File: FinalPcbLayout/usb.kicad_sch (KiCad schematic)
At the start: 5 parts, among them J5 USB_C_Receptacle, Q2 S8050, Q3 S8050

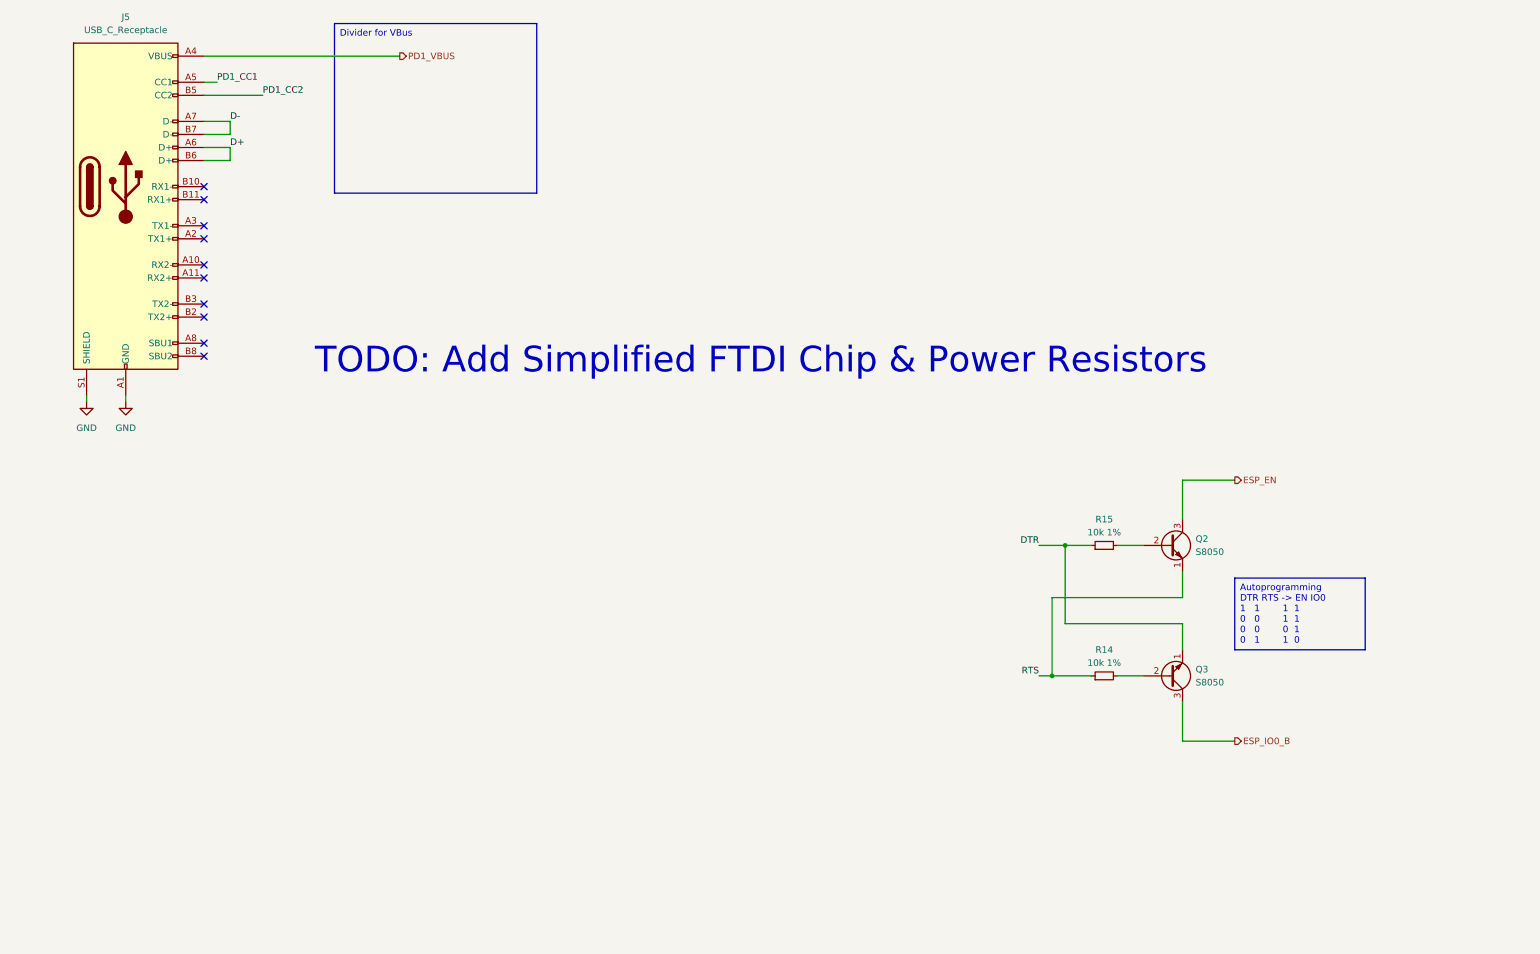
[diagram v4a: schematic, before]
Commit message: Found A Good USB-To-Uart
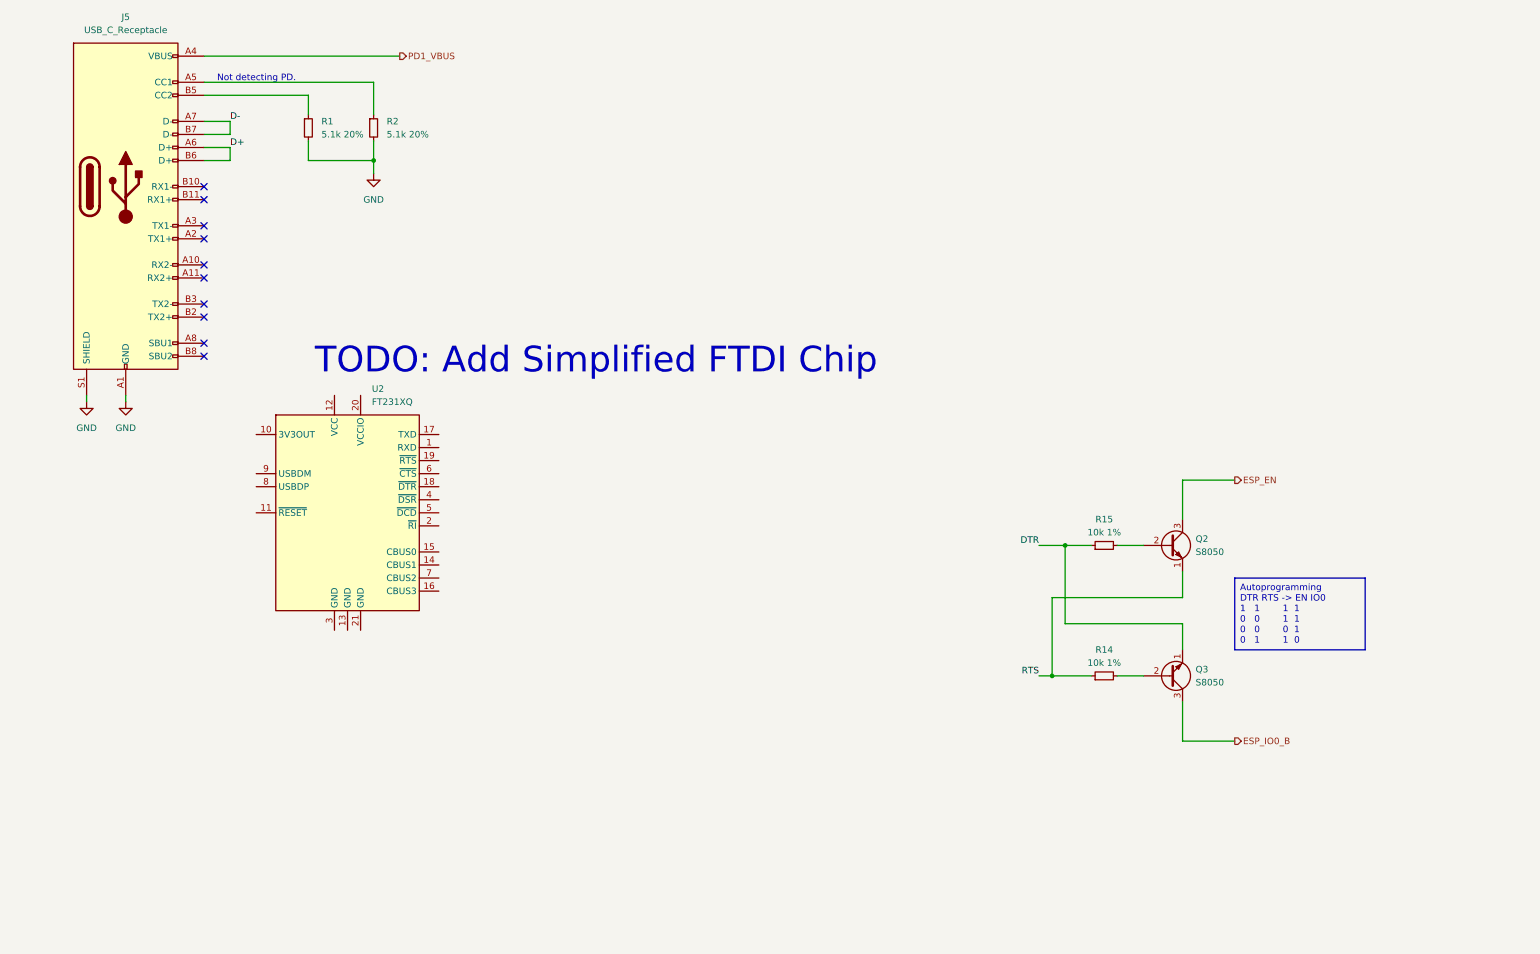
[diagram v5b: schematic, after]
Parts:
- added R1, R2: 5.1k 20%, symbol Device:R_Small
- added U2: FT231XQ, Package_DFN_QFN:QFN-20-1EP_4x4mm_P0.5mm_EP2.5x2.5mm, symbol Interface_USB:FT231XQ
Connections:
- net GND: now also R1.2, R2.2
- net PD1_CC1: no longer names the net of J5.A5 (CC1)
- net PD1_CC1: now also R2.1
- net PD1_CC2: no longer names the net of J5.B5 (CC2)
- net PD1_CC2: now also R1.1
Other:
- note added: "Not detecting PD."
- note added: "TODO: Add Simplified FTDI Chip"
- note removed: "TODO: Add Simplified FTDI Chip & Power Resistors"
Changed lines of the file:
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@@
     (comment 1 "Author: Jake Armstrong")
+  )
+  (junction (at 83.82 41.91) (diameter 0) (color 0 0 0 0)
   )
   (junction (at 215.9 142.24) (diameter 0) (color 0 0 0 0)
@@
     (stroke (width 0) (type default))
   )
+  (wire (pts (xy 71.12 38.1) (xy 71.12 41.91))
+    (stroke (width 0) (type default))
+  )
   (wire (pts (xy 251.46 154.94) (xy 241.3 154.94))
     (stroke (width 0) (type default))
   )
+  (wire (pts (xy 83.82 38.1) (xy 83.82 41.91))
+    (stroke (width 0) (type default))
+  )
+  (wire (pts (xy 83.82 41.91) (xy 83.82 44.45))
+    (stroke (width 0) (type default))
+  )
   (wire (pts (xy 55.88 34.29) (xy 50.8 34.29))
     (stroke (width 0) (type default))
@@
     (stroke (width 0) (type default))
   )
+  (wire (pts (xy 71.12 33.02) (xy 71.12 29.21))
+    (stroke (width 0) (type default))
+  )
+  (wire (pts (xy 71.12 41.91) (xy 83.82 41.91))
+    (stroke (width 0) (type default))
+  )
   (wire (pts (xy 50.8 36.83) (xy 55.88 36.83))
     (stroke (width 0) (type default))
@@
     (stroke (width 0) (type default))
   )
-  (wire (pts (xy 50.8 29.21) (xy 62.23 29.21))
+  (wire (pts (xy 50.8 29.21) (xy 71.12 29.21))
     (stroke (width 0) (type default))
   )
@@
     (stroke (width 0) (type default))
   )
+  (wire (pts (xy 83.82 26.67) (xy 83.82 33.02))
+    (stroke (width 0) (type default))
+  )
   (wire (pts (xy 55.88 39.37) (xy 50.8 39.37))
     (stroke (width 0) (type default))
@@
     (stroke (width 0) (type default))
   )
-  (wire (pts (xy 50.8 26.67) (xy 53.34 26.67))
+  (wire (pts (xy 50.8 26.67) (xy 83.82 26.67))
     (stroke (width 0) (type default))
   )
@@
     (effects (font (size 1.27 1.27)) (justify left top))
   )
-  (text_box "Divider for VBus\n"
-    (at 76.2 15.24 0) (size 39.37 33.02)
-    (stroke (width 0) (type default))
-    (fill (type none))
-    (effects (font (size 1.27 1.27)) (justify left top))
-  )
-  (text "TODO: Add Simplified FTDI Chip & Power Resistors" (at 72.39 83.82 0)
+  (text "TODO: Add Simplified FTDI Chip\n" (at 72.39 83.82 0)
     (effects (font (size 5 5)) (justify left bottom))
+  )
+  (text "Not detecting PD.\n" (at 53.34 26.67 0)
+    (effects (font (size 1.27 1.27)) (justify left bottom))
   )
   (label "D+" (at 55.88 39.37 0) (fields_autoplaced)
@@
     (effects (font (size 1.27 1.27)) (justify right bottom))
   )
-  (label "PD1_CC2" (at 62.23 29.21 0) (fields_autoplaced)
-    (effects (font (size 1.27 1.27)) (justify left bottom))
-  )
   (label "D-" (at 55.88 34.29 0) (fields_autoplaced)
     (effects (font (size 1.27 1.27)) (justify left bottom))
@@
     (effects (font (size 1.27 1.27)) (justify right bottom))
   )
-  (label "PD1_CC1" (at 53.34 26.67 0) (fields_autoplaced)
-    (effects (font (size 1.27 1.27)) (justify left bottom))
-  )
   (hierarchical_label "ESP_IO0_B" (shape output) (at 251.46 154.94 0) (fields_autoplaced)
     (effects (font (size 1.27 1.27)) (justify left))
@@
         (path "/9fcc273e-b318-4ade-b4c7-fe4ddbf9d677/80fb5872-9ff7-41e5-9921-84d432e9852e"
           (reference "Q3") (unit 1)
+        )
+      )
+    )
+  )
+  (symbol (lib_id "power:GND") (at 83.82 44.45 0) (unit 1)
+    (in_bom yes) (on_board yes) (dnp no) (fields_autoplaced)
+    (property "Reference" "#PWR06" (at 83.82 50.8 0)
+      (effects (font (size 1.27 1.27)) hide)
+    )
+    (property "Value" "GND" (at 83.82 49.53 0)
+      (effects (font (size 1.27 1.27)))
+    )
+    (property "Footprint" "" (at 83.82 44.45 0)
+      (effects (font (size 1.27 1.27)) hide)
+    )
+    (property "Datasheet" "" (at 83.82 44.45 0)
+      (effects (font (size 1.27 1.27)) hide)
+    )
+    (pin "1")
+    (instances
+      (project "FinalPcbLayout"
+        (path "/9fcc273e-b318-4ade-b4c7-fe4ddbf9d677/80fb5872-9ff7-41e5-9921-84d432e9852e"
+          (reference "#PWR06") (unit 1)
         )
       )
@@
     )
   )
+  (symbol (lib_id "Device:R_Small") (at 83.82 35.56 0) (unit 1)
+    (in_bom yes) (on_board yes) (dnp no) (fields_autoplaced)
+    (property "Reference" "R2" (at 86.36 34.29 0)
+      (effects (font (size 1.27 1.27)) (justify left))
+    )
+    (property "Value" "5.1k 20%" (at 86.36 36.83 0)
+      (effects (font (size 1.27 1.27)) (justify left))
+    )
+    (property "Footprint" "" (at 83.82 35.56 0)
+      (effects (font (size 1.27 1.27)) hide)
+    )
+    (property "Datasheet" "~" (at 83.82 35.56 0)
+      (effects (font (size 1.27 1.27)) hide)
+    )
+    (pin "2")
+    (pin "1")
+    (instances
+      (project "FinalPcbLayout"
+        (path "/9fcc273e-b318-4ade-b4c7-fe4ddbf9d677/80fb5872-9ff7-41e5-9921-84d432e9852e"
+          (reference "R2") (unit 1)
+        )
+      )
+    )
+  )
   (symbol (lib_id "power:GND") (at 27.94 88.9 0) (unit 1)
     (in_bom yes) (on_board yes) (dnp no) (fields_autoplaced)
@@
         (path "/9fcc273e-b318-4ade-b4c7-fe4ddbf9d677/80fb5872-9ff7-41e5-9921-84d432e9852e"
           (reference "R14") (unit 1)
+        )
+      )
+    )
+  )
+  (symbol (lib_id "Device:R_Small") (at 71.12 35.56 0) (unit 1)
+    (in_bom yes) (on_board yes) (dnp no) (fields_autoplaced)
+    (property "Reference" "R1" (at 73.66 34.29 0)
+      (effects (font (size 1.27 1.27)) (justify left))
+    )
+    (property "Value" "5.1k 20%" (at 73.66 36.83 0)
+      (effects (font (size 1.27 1.27)) (justify left))
+    )
+    (property "Footprint" "" (at 71.12 35.56 0)
+      (effects (font (size 1.27 1.27)) hide)
+    )
+    (property "Datasheet" "~" (at 71.12 35.56 0)
+      (effects (font (size 1.27 1.27)) hide)
+    )
+    (pin "2")
+    (pin "1")
+    (instances
+      (project "FinalPcbLayout"
+        (path "/9fcc273e-b318-4ade-b4c7-fe4ddbf9d677/80fb5872-9ff7-41e5-9921-84d432e9852e"
+          (reference "R1") (unit 1)
         )
       )
@@
         )
       )
+    )
+  )
+  (symbol (lib_id "Interface_USB:FT231XQ") (at 78.74 110.49 0) (unit 1)
+    (in_bom yes) (on_board yes) (dnp no) (fields_autoplaced)
+    (property "Reference" "U2" (at 83.4741 86.36 0)
+      (effects (font (size 1.27 1.27)) (justify left))
+    )
+    (property "Value" "FT231XQ" (at 83.4741 88.9 0)
+      (effects (font (size 1.27 1.27)) (justify left))
+    )
+    (property "Footprint" "Package_DFN_QFN:QFN-20-1EP_4x4mm_P0.5mm_EP2.5x2.5mm" (at 113.03 130.81 0)
+      (effects (font (size 1.27 1.27)) hide)
+    )
+    (property "Datasheet" "https://www.ftdichip.com/Support/Documents/DataSheets/ICs/DS_FT231X.pdf" (at 78.74 110.49 0)
+      (effects (font (size 1.27 1.27)) hide)
+    )
+    (property "digikey_pn" "768-1155-ND" (at 78.74 110.49 0)
+      (effects (font (size 1.27 1.27)) hide)
+    )
+    (pin "12")
+    (pin "4")
+    (pin "19")
+    (pin "9")
+    (pin "15")
+    (pin "13")
+    (pin "1")
+    (pin "20")
+    (pin "17")
+    (pin "11")
+    (pin "2")
+    (pin "21")
+    (pin "3")
+    (pin "10")
+    (pin "5")
+    (pin "6")
+    (pin "7")
+    (pin "14")
+    (pin "16")
+    (pin "18")
+    (pin "8")
+    (instances
+      (project "FinalPcbLayout"
+        (path "/9fcc273e-b318-4ade-b4c7-fe4ddbf9d677/80fb5872-9ff7-41e5-9921-84d432e9852e"
+          (reference "U2") (unit 1)
+        )
+      )

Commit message: Working on USB to UART
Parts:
- R1, R2: footprint (none) -> Resistor_SMD:R_0603_1608Metric
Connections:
- net D+: now also U2.8 (USBDP)
- net D-: now also U2.9 (USBDM)
- net DTR: now also U2.18 (~{DTR})
- net GND: now also U2.13 (GND), U2.21 (GND), U2.3 (GND)
- net RTS: now also U2.19 (~{RTS})
- net +3V3: now reaches U2.10 (3V3OUT)
- net +3V3: now also U2.11 (~{RESET}), U2.12 (VCC), U2.20 (VCCIO)
- no-connect marks 10 -> 14
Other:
- note removed: "TODO: Add Simplified FTDI Chip"
- moved on the sheet: U2
